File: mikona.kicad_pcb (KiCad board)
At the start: 4 copper layers, 50 x 40 mm, 83 parts, among them J1 TC2030-IDC-NL, Q1 BSC109N10NS3 G, Q2 FQD5N60C, Q3 IGB50N60T, Q4 IGB50N60T, U1 LT3750EMS#PBF, U10 24CW1280T, U2 ZXGD3009E6, U3 MCP6V51, U4 STM32F103T6U6A, U5 Texas Instruments UCC27624DR, U6 KTD2052, U7 TLT9251VLE, U8 MAX17671FATB+, U9 MCP4562T-503E/MF

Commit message: Cleanup the project after moving to KiCad.
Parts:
- removed R18, R27, R28, R29, R30: 100K, Vault:RESC1005X40X25ML10T10
- removed R20, R21: 10, Vault:RESC1005X40X25NL05T05
- removed R23: 787K, Vault:RESC1005X40X25LL05T05
- removed R25, R26: 4.7K, Vault:RESC1005X40X25NL05T05
- added C28: 22uF, Capacitor_SMD:C_0805_2012Metric_Pad1.18x1.45mm_HandSolder, B.Cu at (184.1, 114.2)
- added C29: 2.2uF, Capacitor_SMD:C_0402_1005Metric_Pad0.74x0.62mm_HandSolder, B.Cu at (190.4, 114.5)
- added D5: SMBJ13CA, Diode_SMD:D_SMB_Handsoldering, B.Cu at (176.3, 92.2)
- added RN1: 100K, Resistor_SMD:R_Array_Convex_2x0402, F.Cu at (109.8, 103.2)
- added RN2: 4.7K, Resistor_SMD:R_Array_Convex_2x0402, F.Cu at (107.5, 106.5)
- added RN3: 100K, Resistor_SMD:R_Array_Convex_2x0402, F.Cu at (107.2, 108.5)
- added U11: MIC5528-3.3, MIC5528-3.3YMT-TR:SON40P120X120X60-7N, B.Cu at (188.7, 114.4)
- C1, C12: value 10 µF -> 10µF; footprint Vault:RESC2013X55X40ML15T20 -> Capacitor_SMD:C_0805_2012Metric_Pad1.18x1.45mm_HandSolder
- C10, C14, C15, C16, C18, C19, C20, C27: footprint Vault:PCB-ya5qsrmvtd5pjczft90h-1 -> Capacitor_SMD:C_0402_1005Metric_Pad0.74x0.62mm_HandSolder
- C11: footprint Vault:PCB-lqeomw61a722wi99q4vw-1 -> Capacitor_SMD:C_0402_1005Metric_Pad0.74x0.62mm_HandSolder
- C13: value 100nF -> 10µF; footprint Vault:PCB-ya5qsrmvtd5pjczft90h-1 -> Capacitor_SMD:C_0805_2012Metric_Pad1.18x1.45mm_HandSolder
- C17: footprint Vault:PCB-8tuutlkq7p1aj3t2dfdp-1 -> Capacitor_SMD:C_0402_1005Metric_Pad0.74x0.62mm_HandSolder
- C2: footprint Vault:PCB-nvrhrmzuvt0gp2xpn124-1 -> Capacitor_SMD:C_1206_3216Metric_Pad1.33x1.80mm_HandSolder
- C21: footprint Vault:PCB-lqeomw61a722wi99q4vw-1 -> Capacitor_SMD:C_0805_2012Metric_Pad1.18x1.45mm_HandSolder
- C22: value 10 µF -> 100nF; footprint Vault:RESC2013X55X40ML15T20 -> Capacitor_SMD:C_0402_1005Metric_Pad0.74x0.62mm_HandSolder; moved to F.Cu
- C23: footprint Vault:PCB-cxx7a5qu32qlaf9eltup-1 -> Capacitor_SMD:C_0402_1005Metric_Pad0.74x0.62mm_HandSolder
- C24: value 1uF -> 10uF; footprint Vault:CAPC1608X90X35ML15T15 -> Capacitor_SMD:C_0603_1608Metric_Pad1.08x0.95mm_HandSolder
- C25: footprint Vault:CAPC1608X90X35LL10T15 -> Capacitor_SMD:C_0402_1005Metric_Pad0.74x0.62mm_HandSolder
- C26: value 4.7uF -> 22uF; footprint Vault:CAPC1608X90X35NL10T15 -> Capacitor_SMD:C_0805_2012Metric_Pad1.18x1.45mm_HandSolder
- C3, C9: footprint Vault:PCB-fmxckod8eunvntzfi285-1 -> Capacitor_SMD:C_0402_1005Metric_Pad0.74x0.62mm_HandSolder
- C4, C5, C6: value 22 uF -> 22uF; footprint Vault:CAPC3225X270X30NL30 -> Capacitor_SMD:C_1210_3225Metric_Pad1.33x2.70mm_HandSolder
- C7: footprint Vault:PCBComponent_1 -> Capacitor_SMD:CP_Elec_8x11.9
- C8: footprint Vault:PCB-hxcivebo8v2ep67jp7i8-1 -> Capacitor_SMD:C_1812_4532Metric_Pad1.57x3.40mm_HandSolder
- D1: footprint Vault:PCB-1avwftqup47cwryg2qb4-1 -> Diode_SMD:D_SMB_Handsoldering
- D2: value SP712 -> SMBJ13CA; footprint Vault:ONSC-SOT-23-3-318-08_V -> Diode_SMD:D_SMB_Handsoldering
- D3: value onsemi FFSB2065BDN-F085 -> FFSB2065BDN-F085; footprint Vault:ONSC-TO-263-2L-3_V -> Package_TO_SOT_SMD:TO-263-2
- D4: value Lite-On LTST-C19HE1WT -> RGB; footprint Vault:PCB-52d9enhv62acg8agpph7-1 -> LED_SMD:LED_LiteOn_LTST-C19HE1WT
- F1: footprint Vault:PCB-177u4nhbl1z1alzoqvvf-1 -> Fuse:Fuse_0603_1608Metric_Pad1.05x0.95mm_HandSolder
- FB2: value 100 -> FerriteBead_Small; footprint Vault:MURA-BLM18KG_TN-B60-CHIP-2_V3 -> Resistor_SMD:R_0603_1608Metric_Pad0.98x0.95mm_HandSolder
- J1: footprint Vault:PCB-ltb50y2q1twco73v61fe-1 -> Connector:Tag-Connect_TC2030-IDC-NL_2x03_P1.27mm_Vertical
- JCAP1: renamed from JCAP; footprint Vault:PCB-udjxl8ocgqbbk8gqzxxz-1 -> 1054291104:MOLEX_1054291104
- JMAG1: renamed from JMAG; footprint Vault:PCB-udjxl8ocgqbbk8gqzxxz-1 -> 1054291104:MOLEX_1054291104
- JMAIN1: renamed from JMAIN; footprint Vault:PCB-udjxl8ocgqbbk8gqzxxz-1 -> 1054291104:MOLEX_1054291104
- L1: value Coilcraft DA2034-ALB -> DA2034-AL; footprint Vault:LCC18 -> DA2034-AL:DA2034-AL
- L2: value 68.0µH -> 4.7uH; footprint Vault:PCB-o31o4oqkad523pnvsppd-1 -> Inductor_SMD:L_Taiyo-Yuden_NR-50xx_HandSoldering
- Q1: value BSC109N10NS3 G -> BSC109N10NS3G; footprint Vault:INF-PG-TDSON-8-1_V -> Package_TO_SOT_SMD:TDSON-8-1
- Q2: value FQD5N60C -> STN3N40K3; footprint Vault:PCB-yetu4xpugvmduszhgs8y-1 -> Package_TO_SOT_SMD:SOT-223
- Q3, Q4: footprint Vault:INF-PG-TO-263-3-2_A_M -> Package_TO_SOT_SMD:TO-263-2
- R1: footprint Vault:RESC1005X40X25ML05T05 -> Resistor_SMD:R_0402_1005Metric_Pad0.72x0.64mm_HandSolder
- R10, R11, R9: footprint Vault:Panasonic ERJ-1TNF22R6U-Footprint-1 -> Resistor_SMD:R_2512_6332Metric_Pad1.40x3.35mm_HandSolder
- R12, R2, R3, R6: footprint Vault:RESC1005X40X25ML10T10 -> Resistor_SMD:R_0402_1005Metric_Pad0.72x0.64mm_HandSolder
- R13: value 100K -> 0; footprint Vault:RESC1005X40X25ML10T10 -> Resistor_SMD:R_0402_1005Metric_Pad0.72x0.64mm_HandSolder
- R14: footprint Vault:SMD0603GRID25PAD90 -> Resistor_SMD:R_0603_1608Metric_Pad0.98x0.95mm_HandSolder
- R15: footprint Vault:ERJ-PB3B1002V -> Resistor_SMD:R_0603_1608Metric_Pad0.98x0.95mm_HandSolder
- R16: footprint Vault:CAPC1608X90X35LL15T15 -> Resistor_SMD:R_0603_1608Metric_Pad0.98x0.95mm_HandSolder
- R17: value 0 -> 10; footprint Vault:RESC1005X40X25ML05T10 -> Resistor_SMD:R_0402_1005Metric_Pad0.72x0.64mm_HandSolder
- R19: footprint Vault:RESC1005X37X25LL05T10 -> Resistor_SMD:R_0402_1005Metric_Pad0.72x0.64mm_HandSolder
- R22, R5: footprint Vault:RESC1005X40X25ML05T10 -> Resistor_SMD:R_0402_1005Metric_Pad0.72x0.64mm_HandSolder
- R24: value 3.32M -> 0; footprint Vault:RESC1005X40X25NL05T05 -> Resistor_SMD:R_0402_1005Metric_Pad0.72x0.64mm_HandSolder; moved to F.Cu
- R4: value 100K -> 10; footprint Vault:RESC1005X40X25ML10T10 -> Resistor_SMD:R_0402_1005Metric_Pad0.72x0.64mm_HandSolder
- R7: footprint Vault:PCB-lktu9k9qvhh1xmnw65nf-1 -> Resistor_SMD:R_0805_2012Metric_Pad1.20x1.40mm_HandSolder
- R8: footprint Vault:RESC1005X40X25NL05T05 -> Resistor_SMD:R_0402_1005Metric_Pad0.72x0.64mm_HandSolder
- U1: value LT3750EMS#PBF -> LT3750EMSTR; footprint Vault:LT-MS-10_N -> LT3750EMSTR:MSOP-10_MS
- U10: value 24CW1280T -> MX25V1006FZUI; footprint Vault:PCB-du7oa82jyfofml92o6ch-1 -> MX25V1006FZUI:MX25V1006FZUI
- U2: footprint Vault:MF06A_N -> Package_TO_SOT_SMD:SOT-23-6
- U3: value MCP6V51 -> NCS325; footprint Vault:ADI-RJ-5_L -> Package_TO_SOT_SMD:SOT-23-5
- U4: value STM32F103T6U6A -> STM32F042G6Ux; footprint Vault:STM-VFQFPN36_L -> Package_DFN_QFN:QFN-28_4x4mm_P0.5mm
- U5: value Texas Instruments UCC27624DR -> IX4427MTR; footprint Vault:SOIC-OA8_L -> Package_DFN_QFN:VDFN-8-1EP_2x2mm_P0.5mm_EP0.9x1.7mm
- U6: value KTD2052 -> KTD2026EWE-TR; footprint Vault:PCB-1zdkv4te5dlcf1e3m0hc-1 -> KTD2026EWE-TR:SON40P150X150X55-9N
- U7: value TLT9251VLE -> ATA6561-GBQW; footprint Vault:PCB-is4r40753zstvrjiqh7i-1 -> ATA6561-GBQW:SON65P300X300X100-9N
- U8: value MAX17671FATB+ -> AP63205WU; footprint Vault:T1033+1_V -> Package_TO_SOT_SMD:TSOT-23-6
- U9: value MCP4562T-503E/MF -> MCP4562T-503E; footprint Vault:DFN-MF8 -> MCP4562T-503E_MF:SON65P300X300X100-9N-D
- moved R13 51.6 mm to (188.7, 115.8), turned to 180 degrees
- moved C22 38.5 mm to (183.8, 117.6)
- moved R4 27.1 mm to (153.5, 100.0)
- moved FB2 23.9 mm to (189.7, 118.1)
- moved C24 21.7 mm to (188.1, 118.1)
- moved R17 19.6 mm to (153.5, 99.0)
- moved D2 19.2 mm to (176.1, 103.8), turned to 90 degrees
- moved R24 17.9 mm to (186.1, 118.6), turned to -90 degrees
- moved C25 17.0 mm to (188.7, 113.1), turned to 0 degrees
- moved C26 16.4 mm to (186.1, 114.2), turned to 90 degrees
- moved U8 15.6 mm to (185.0, 118.1), turned to 180 degrees
- moved L2 12.5 mm to (180.2, 116.0), turned to 90 degrees
- moved JCAP1 3.05 mm to (166.7, 90.8)
- moved JMAG1 2.97 mm to (166.7, 98.5)
- moved JMAIN1 2.59 mm to (166.7, 120.3)
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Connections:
- net NetD1_2 renamed Net-(D1-A)
- net NetD4_1 renamed Net-(D4-RK)
- net NetF1_1 renamed Net-(F1-Pad1)
- net NetQ1_4 renamed Net-(Q1-G)
- net NetR23_2 renamed Net-(U8-EN)
- net RVOUT renamed /Power/RVOUT
- C1 pad 1: GND -> +24V
- C1 pad 2: VIN -> GND
- C10 pad 1: GND -> +3.3V
- C10 pad 2: 3V3 -> GND
- C11 pad 1: GND -> Net-(U4-NRST)
- C11 pad 2: NetC11_2 -> GND
- C12 pad 2: 5V -> +5V
- C13 pad 1: GND -> +24V
- C13 pad 2: 3V3 -> GND
- C14 pad 1: GND -> +3.3V
- C14 pad 2: 3V3 -> GND
- C15 pad 1: GND -> +3.3V
- C15 pad 2: 3V3 -> GND
- C16 pad 1: GND -> +3.3V
- C16 pad 2: 3V3 -> GND
- C17 pad 1: GND -> +3.3V
- C17 pad 2: 3V3 -> GND
- C18 pad 1: GND -> +3.3V
- C18 pad 2: 3V3 -> GND
- C19 pad 1: GND -> +3.3V
- C19 pad 2: 3V3 -> GND
- C2 pad 1: NetC2_1 -> GND
- C2 pad 2: GND -> Net-(U1-VTRANS)
- C20 pad 1: GND -> +5V
- C20 pad 2: 5V -> GND
- C21 pad 1: GND -> +24V
- C21 pad 2: VIN -> GND
- C22 pad 1: GND -> Net-(U8-BST)
- C22 pad 2: VIN -> Net-(U8-SW)
- C23 pad 1: GND -> +24V
- C23 pad 2: VIN -> GND
- C24 pad 1: GND -> Net-(U8-IN)
- C24 pad 2: NetC24_2 -> GND
- C25 pad 1: GND -> +5V
- C25 pad 2: 3V3 -> GND
- C26 pad 1: GND -> +5V
- C26 pad 2: 5V -> GND
- C27 pad 1: GND -> +3.3V
- C27 pad 2: 3V3 -> GND
- C3 pad 1: GND -> Net-(U1-RBG)
- C3 pad 2: NetC3_2 -> GND
- C4 pad 2: VIN -> +24V
- C5 pad 2: VIN -> +24V
- C6 pad 2: VIN -> +24V
- C7 pad 1: VIN -> +24V
- C8 pad 1: GND -> +3.3V
- C8 pad 2: VOUT -> GND
- C9 pad 1: GND -> Net-(U3-+)
- C9 pad 2: NetC9_2 -> GND
- D1 pad 1: VOUT -> +3.3V
- D2 pad 1: NetD2_1 -> Net-(D2-A1)
- D2 pad 2: NetD2_2 -> GND
- D3 pad 1: MAGNET_B_2 -> /MAGNET_A_2
- D3 pad 2: VOUT -> +3.3V
- D3 pad 3: MAGNET_A_2 -> /MAGNET_B_2
- D4 pad 2: NetD4_2 -> Net-(D4-GK)
- D4 pad 3: NetD4_3 -> Net-(D4-BK)
- D4 pad 4: NetD4_4 -> +5V
- F1 pad 2: VIN -> +24V
- FB2 pad 1: VIN -> +24V
- FB2 pad 2: NetC24_2 -> Net-(U8-IN)
- J1 pad 1: 3V3 -> +3.3V
- J1 pad 2: SWDIO -> /Logic/SWDIO
- J1 pad 3: SW_NRST -> /Logic/SW_NRST
- J1 pad 4: SWCLK -> /Logic/SWCLK
- J1 pad 6: SWO -> unconnected-(J1-SWO-Pad6)
- JCAP1 pad 3: VOUT -> +3.3V
- JCAP1 pad 4: VOUT -> +3.3V
- JMAG1 pad 1: MAGNET_A_2 -> /MAGNET_A_2
- JMAG1 pad 2: MAGNET_B_2 -> /MAGNET_B_2
- JMAG1 pad 3: VOUT -> +3.3V
- JMAG1 pad 4: VOUT -> +3.3V
- JMAIN1 pad 1: CAN_P -> /CAN_P
- JMAIN1 pad 2: CAN_N -> /CAN_N
- L1 pad 10: NMOS_DRAIN -> /Power/NMOS_DRAIN
- L1 pad 3: VIN -> +24V
- L1 pad 4: VIN -> +24V
- L1 pad 5: VIN -> +24V
- L1 pad 6: VIN -> +24V
- L1 pad 7: NMOS_DRAIN -> /Power/NMOS_DRAIN
- L1 pad 8: NMOS_DRAIN -> /Power/NMOS_DRAIN
- L1 pad 9: NMOS_DRAIN -> /Power/NMOS_DRAIN
- L2 pad 1: NetL2_1 -> Net-(U8-SW)
- L2 pad 2: 5V -> +5V
- Q1 pad 1: NetQ1_1 -> Net-(U1-SOURCE)
- Q1 pad 2: NetQ1_1 -> Net-(U1-SOURCE)
- Q1 pad 3: NetQ1_1 -> Net-(U1-SOURCE)
- Q1 pad 5: NMOS_DRAIN -> /Power/NMOS_DRAIN
- Q2 pad 1: NetQ2_1 -> Net-(Q2-G)
- Q2 pad 4: NetQ2_4 -> Net-(Q2-D-Pad2)
- Q3 pad 1: NetD2_1 -> Net-(D2-A1)
- Q3 pad 2: MAGNET_A_2 -> /MAGNET_A_2
- Q4 pad 1: NetD2_2 -> Net-(D5-A1)
- Q4 pad 2: MAGNET_B_2 -> /MAGNET_B_2
- R1 pad 1: NetR1_1 -> /Power/NMOS_DRAIN
- R1 pad 2: NMOS_DRAIN -> Net-(U1-RDCM)
- R10 pad 1: VOUT -> +3.3V
- R10 pad 2: NetQ2_4 -> Net-(Q2-D-Pad2)
- R11 pad 1: VOUT -> +3.3V
- R11 pad 2: NetQ2_4 -> Net-(Q2-D-Pad2)
- R12 pad 1: GND -> Net-(U2-SINK)
- R12 pad 2: NetR8_1 -> GND
- R13 pad 1: GND -> +5V
- R13 pad 2: DISCHARGE -> Net-(U11-EN)
- R14 pad 1: NetR14_1 -> +3.3V
- R14 pad 2: VOUT -> Net-(R14-Pad2)
- R15 pad 1: GND -> Net-(R14-Pad2)
- R15 pad 2: NetR14_1 -> GND
- R16 pad 1: NetR14_1 -> Net-(U3-+)
- R16 pad 2: NetC9_2 -> Net-(R14-Pad2)
- R17 pad 1: NetC11_2 -> Net-(D5-A1)
- R17 pad 2: REG_NRST -> Net-(U5-OUT_B)
- R19 pad 1: CAN_N -> /CAN_P
- R19 pad 2: CAN_P -> /CAN_N
- R2 pad 1: 3V3 -> +5V
- R2 pad 2: DONE -> Net-(U6-ST)
- R22 pad 1: SW_NRST -> Net-(U4-NRST)
- R22 pad 2: NetC11_2 -> /Logic/SW_NRST
- R24 pad 2: NetC24_2 -> Net-(U8-IN)
- R3 pad 1: NetR3_1 -> /Power/NMOS_DRAIN
- R3 pad 2: NMOS_DRAIN -> Net-(U9-P0B)
- R4 pad 1: GND -> Net-(D2-A1)
- R4 pad 2: CHARGE -> Net-(U5-OUT_A)
- R5 pad 1: VIN -> +24V
- R5 pad 2: NetC2_1 -> Net-(U1-VTRANS)
- R6 pad 1: GND -> Net-(U1-RBG)
- R6 pad 2: NetC3_2 -> GND
- R7 pad 1: GND -> Net-(U1-SOURCE)
- R7 pad 2: NetQ1_1 -> GND
- R8 pad 1: NetR8_1 -> Net-(Q2-G)
- R8 pad 2: NetQ2_1 -> Net-(U2-SINK)
- R9 pad 1: VOUT -> +3.3V
- R9 pad 2: NetQ2_4 -> Net-(Q2-D-Pad2)
- U1 pad 1: NetC2_1 -> Net-(U1-VTRANS)
- U1 pad 10: NetC3_2 -> Net-(U1-RBG)
- U1 pad 2: DONE -> /Logic/DONE
- U1 pad 3: CHARGE -> /Logic/CHARGE
- U1 pad 4: VIN -> +24V
- U1 pad 6: NetQ1_1 -> Net-(U1-SOURCE)
- U1 pad 8: NetR1_1 -> Net-(U1-RDCM)
- U10 pad 1: SCL -> /Logic/FLASH_CS
- U10 pad 2: GND -> /Logic/MISO
- U10 pad 3: SDA -> /Logic/FLASH_WP
- U10 pad 4: 3V3 -> GND
- U10 pad 5: (no net) -> /Logic/MOSI
- U2 pad 1: VIN -> +24V
- U2 pad 2: DISCHARGE -> /Logic/DISCHARGE
- U2 pad 4: NetR8_1 -> Net-(U2-SINK)
- U2 pad 5: (no net) -> unconnected-(U2-NC-Pad5)
- U2 pad 6: NetR8_1 -> Net-(U2-SINK)
- U3 pad 1: VOUT_ADC -> /Logic/VOUT_ADC
- U3 pad 3: NetC9_2 -> Net-(U3-+)
- U3 pad 4: VOUT_ADC -> /Logic/VOUT_ADC
- U3 pad 5: 3V3 -> +3.3V
- U4 pad 1: 3V3 -> unconnected-(U4-PB8-Pad1)
- U4 pad 10: (no net) -> /Logic/KICK_B
- U4 pad 11: (no net) -> /Logic/KICK_A
- U4 pad 12: DISCHARGE -> unconnected-(U4-PA6-Pad12)
- U4 pad 13: VOUT_ADC -> unconnected-(U4-PA7-Pad13)
- U4 pad 14: KICK_B -> unconnected-(U4-PB0-Pad14)
- U4 pad 15: KICK_A -> /Logic/CAN_STB
- U4 pad 16: KICK_A_EN -> GND
- U4 pad 17: KICK_B_EN -> +3.3V
- U4 pad 18: GND -> +3.3V
- U4 pad 19: 3V3 -> /Logic/CAN_RX
- U4 pad 2: (no net) -> /Logic/SDA
- U4 pad 20: (no net) -> /Logic/CAN_TX
- U4 pad 21: (no net) -> /Logic/SWDIO
- U4 pad 22: CAN_STB -> /Logic/SWCLK
- U4 pad 23: CAN_RX -> unconnected-(U4-PA15-Pad23)
- U4 pad 24: CAN_TX -> /Logic/SCK
- U4 pad 25: SWDIO -> /Logic/MISO
- U4 pad 26: GND -> /Logic/MOSI
- U4 pad 27: 3V3 -> /Logic/FLASH_CS
- U4 pad 28: SWCLK -> /Logic/FLASH_WP
- U4 pad 3: (no net) -> /Logic/SCL
- U4 pad 4: NetC11_2 -> Net-(U4-NRST)
- U4 pad 5: GND -> +3.3V
- U4 pad 6: 3V3 -> /Logic/CHARGE
- U4 pad 7: CHARGE -> /Logic/DONE
- U4 pad 8: DONE -> /Logic/DISCHARGE
- U4 pad 9: (no net) -> /Logic/VOUT_ADC
- U5 pad 1: KICK_A_EN -> unconnected-(U5-NC-Pad1)
- U5 pad 2: KICK_A -> /Logic/KICK_A
- U5 pad 4: KICK_B -> /Logic/KICK_B
- U5 pad 5: NetR21_1 -> Net-(U5-OUT_B)
- U5 pad 6: VIN -> +24V
- U5 pad 7: NetR20_1 -> Net-(U5-OUT_A)
- U5 pad 8: KICK_B_EN -> unconnected-(U5-NC-Pad8)
- U6 pad 1: SCL -> Net-(U6-ST)
- U6 pad 2: SDA -> Net-(D4-BK)
- U6 pad 3: NetD4_3 -> Net-(D4-GK)
- U6 pad 5: NetD4_2 -> +5V
- U6 pad 6: NetD4_4 -> /Logic/SCL
- U6 pad 7: GND -> /Logic/SDA
- U6 pad 8: 5V -> GND
- U7 pad 1: CAN_TX -> /Logic/CAN_TX
- U7 pad 3: 5V -> +5V
- U7 pad 4: CAN_RX -> /Logic/CAN_RX
- U7 pad 5: 3V3 -> +3.3V
- U7 pad 6: CAN_N -> /CAN_N
- U7 pad 7: CAN_P -> /CAN_P
- U7 pad 8: CAN_STB -> /Logic/CAN_STB
- U8 pad 1: NetC24_2 -> +5V
- U8 pad 3: (no net) -> Net-(U8-IN)
- U8 pad 4: 5V -> GND
- U8 pad 5: 3V3 -> Net-(U8-SW)
- U8 pad 6: 5V -> Net-(U8-BST)
- U9 pad 2: SCL -> /Logic/SCL
- U9 pad 3: SDA -> /Logic/SDA
- U9 pad 6: NetR3_1 -> Net-(U9-P0B)
- U9 pad 8: 3V3 -> +3.3V
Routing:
- net (no net): track 0.00 -> 224.5 mm, vias 0 -> 14
- net MAGNET_B_2: track 34.8 -> 0.00 mm, vias 2 -> 0
- net VOUT: track 34.6 -> 0.00 mm
- net REG_NRST: track 33.3 -> 0.00 mm, vias 1 -> 0
- net SCL: track 26.9 -> 0.00 mm, vias 2 -> 0
- net VIN: track 22.5 -> 0.00 mm
- net /Logic/DISCHARGE: track 0.00 -> 22.2 mm
- net DISCHARGE: track 21.5 -> 0.00 mm
- net NMOS_DRAIN: track 20.6 -> 0.00 mm
- net SDA: track 20.5 -> 0.00 mm, vias 2 -> 0
- net DONE: track 19.5 -> 0.00 mm
- net /Logic/DONE: track 0.00 -> 19.5 mm
- net CHARGE: track 19.5 -> 0.00 mm
- net /Logic/CHARGE: track 0.00 -> 19.5 mm
- net /Logic/VOUT_ADC: track 0.00 -> 17.6 mm
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- removed copper zone on B.Cu, net NetC24_2
- removed copper zone on B.Cu, net VIN

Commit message: Add missing 3d models.
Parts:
- D4: footprint LED_SMD:LED_LiteOn_LTST-C19HE1WT -> LTST-C19HE1WT:LED_LiteOn_LTST-C19HE1WT
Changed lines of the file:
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@@
     (pad "9" smd rect (at 0 0 180) (size 1.6 2.4) (layers "F.Cu" "F.Paste" "F.Mask")
       (net 1 "GND") (pinfunction "EP") (pintype "passive"))
-    (model "MCP4562T-503E_MF.stp"
+    (model "${KIPRJMOD}/libraries/MCP4562T-503E_MF/DFN8_3x3MC_MCH.step"
       (offset (xyz 0 0 0))
       (scale (xyz 1 1 1))
@@
     (pad "S2" smd rect (at 3.055 0.475 270) (size 1.1 10.5) (layers "F.Cu" "F.Paste")
       (net 30 "unconnected-(JMAIN1-SHIELD2-PadS2)") (pinfunction "SHIELD2") (pintype "passive+no_connect"))
+    (model "${KIPRJMOD}/libraries/1054291104/1054291104.step"
+      (offset (xyz 0 0 0))
+      (scale (xyz 1 1 1))
+      (rotate (xyz 0 0 0))
+    )
   )
   (footprint "Resistor_SMD:R_0805_2012Metric_Pad1.20x1.40mm_HandSolder" (layer "F.Cu")
@@
     (pad "9" smd rect (at 0 0 270) (size 0.75 1.25) (layers "F.Cu" "F.Paste" "F.Mask")
       (net 1 "GND") (pinfunction "EP") (pintype "power_in"))
-    (model "KTD2026EWE-TR.stp"
+    (model "${KIPRJMOD}/libraries/KTD2026EWE-TR/UTDFN8_1P5X1P5_KIN.step"
       (offset (xyz 0 0 0))
       (scale (xyz 1 1 1))
@@
     )
   )
-  (footprint "LED_SMD:LED_LiteOn_LTST-C19HE1WT" (layer "F.Cu")
+  (footprint "LTST-C19HE1WT:LED_LiteOn_LTST-C19HE1WT" (layer "F.Cu")
     (at 142.0011 122.0036 -90)
     (descr "LiteOn RGB LED; https://optoelectronics.liteon.com/upload/download/DS22-2008-0044/LTST-C19HE1WT.pdf")
@@
     (pad "4" smd rect (at -0.425 0.725 270) (size 0.65 0.85) (layers "F.Cu" "F.Paste" "F.Mask")
       (net 7 "+5V") (pinfunction "A") (pintype "passive"))
-    (model "${KICAD6_3DMODEL_DIR}/LED_SMD.3dshapes/LED_LiteOn_LTST-C19HE1WT.wrl"
+    (model "${KIPRJMOD}/libraries/LTST-C19HE1WT/LTST-C19HE1WT.STEP"
       (offset (xyz 0 0 0))
       (scale (xyz 1 1 1))
-      (rotate (xyz 0 0 0))
+      (rotate (xyz -90 0 -90))
     )
   )
@@
     (pad "S2" smd rect (at 3.055 0.475 270) (size 1.1 10.5) (layers "F.Cu" "F.Paste")
       (net 26 "unconnected-(JMAG1-SHIELD2-PadS2)") (pinfunction "SHIELD2") (pintype "passive+no_connect"))
+    (model "${KIPRJMOD}/libraries/1054291104/1054291104.step"
+      (offset (xyz 0 0 0))
+      (scale (xyz 1 1 1))
+      (rotate (xyz 0 0 0))
+    )
   )
   (footprint "Capacitor_SMD:C_0402_1005Metric_Pad0.74x0.62mm_HandSolder" (layer "F.Cu")
@@
     (pad "12" smd rect (at 13.46 -7.5 270) (size 3.3 1.27) (layers "F.Cu" "F.Paste" "F.Mask")
       (net 1 "GND") (pinfunction "12") (pintype "passive"))
+    (model "${KIPRJMOD}/libraries/DA2034-AL/Coilcraft-DA2034-AL.step"
+      (offset (xyz 0 0 0))
+      (scale (xyz 1 1 1))
+      (rotate (xyz -90 0 0))
+    )
   )
   (footprint "Connector:Tag-Connect_TC2030-IDC-NL_2x03_P1.27mm_Vertical" (layer "F.Cu")
@@
     (pad "S2" smd rect (at 3.055 0.475 270) (size 1.1 10.5) (layers "F.Cu" "F.Paste")
       (net 24 "unconnected-(JCAP1-SHIELD2-PadS2)") (pinfunction "SHIELD2") (pintype "passive+no_connect"))
+    (model "${KIPRJMOD}/libraries/1054291104/1054291104.step"
+      (offset (xyz 0 0 0))
+      (scale (xyz 1 1 1))
+      (rotate (xyz 0 0 0))
+    )
   )
   (footprint "Capacitor_SMD:C_0402_1005Metric_Pad0.74x0.62mm_HandSolder" (layer "F.Cu")
@@
     (pad "9" smd rect (at 0 0) (size 1.6 2.4) (layers "B.Cu" "B.Mask")
       (net 1 "GND") (pinfunction "EXP") (pintype "power_in"))
+    (model "${KIPRJMOD}/libraries/ATA6561-GBQW/vdfn8-bbb.STEP"
+      (offset (xyz 0 0 0))
+      (scale (xyz 0.5 0.5 0.5))
+      (rotate (xyz 0 0 0))
+    )
   )
   (footprint "Capacitor_SMD:C_0402_1005Metric_Pad0.74x0.62mm_HandSolder" (layer "B.Cu")
@@
         (effects (font (size 1 1) (thickness 0.15)) (justify mirror))
     )
-    (fp_text user "Copyright 2021 Accelerated Designs. All rights reserved." (at 0 0) (layer "Cmts.User")
-        (effects (font (size 0.127 0.127) (thickness 0.002)))
-    )
-    (fp_text user "0.01in/0.255mm" (at 4.4934 0.762) (layer "Cmts.User")
+    (fp_text user "0.02in/0.508mm" (at -4.4934 0.508) (layer "Cmts.User")
         (effects (font (size 1 1) (thickness 0.15)))
     )
-    (fp_text user "0.114in/2.891mm" (at 0 3.4671) (layer "Cmts.User")
+    (fp_text user "0.012in/0.305mm" (at 0 -4.1021) (layer "Cmts.User")
         (effects (font (size 1 1) (thickness 0.15)))
     )
@@
         (effects (font (size 1 1) (thickness 0.15)))
     )
-    (fp_text user "0.02in/0.508mm" (at -4.4934 0.508) (layer "Cmts.User")
+    (fp_text user "0.067in/1.702mm" (at 3.9624 0) (layer "Cmts.User")
         (effects (font (size 1 1) (thickness 0.15)))
     )
-    (fp_text user "0.012in/0.305mm" (at 0 -4.1021) (layer "Cmts.User")
+    (fp_text user "0.114in/2.891mm" (at 0 3.4671) (layer "Cmts.User")
         (effects (font (size 1 1) (thickness 0.15)))
     )
-    (fp_text user "0.067in/1.702mm" (at 3.9624 0) (layer "Cmts.User")
+    (fp_text user "Copyright 2021 Accelerated Designs. All rights reserved." (at 0 0) (layer "Cmts.User")
+        (effects (font (size 0.127 0.127) (thickness 0.002)))
+    )
+    (fp_text user "0.01in/0.255mm" (at 4.4934 0.762) (layer "Cmts.User")
         (effects (font (size 1 1) (thickness 0.15)))
     )
@@
     (pad "9" smd rect (at 0 0 180) (size 0.3048 1.7018) (layers "B.Cu" "B.Paste" "B.Mask")
       (net 1 "GND") (pinfunction "GND") (pintype "power_in"))
+    (model "${KIPRJMOD}/libraries/MX25V1006FZUI/USON8L_MAC.step"
+      (offset (xyz 0 0 0))
+      (scale (xyz 1 1 1))
+      (rotate (xyz 0 0 0))
+    )
   )
   (footprint "Resistor_SMD:R_0402_1005Metric_Pad0.72x0.64mm_HandSolder" (layer "B.Cu")
@@
     (pad "10" smd rect (at 2.1844 1.00076 180) (size 1.397 0.2794) (layers "B.Cu" "B.Paste" "B.Mask")
       (net 4 "Net-(U1-RBG)") (pinfunction "RBG") (pintype "output"))
+    (model "${KIPRJMOD}/libraries/LT3750EMSTR/MSOP-10_MS_LIT.step"
+      (offset (xyz 0 0 0))
+      (scale (xyz 1 1 1))
+      (rotate (xyz 0 0 0))
+    )
   )
   (footprint "Capacitor_SMD:C_0805_2012Metric_Pad1.18x1.45mm_HandSolder" (layer "B.Cu")
@@
     (pad "7" smd rect (at 0 0 180) (size 0.3 0.94) (layers "B.Cu" "B.Mask")
       (net 1 "GND") (pinfunction "GND") (pintype "power_in"))
+    (model "${KIPRJMOD}/libraries/MIC5528-3.3YMT-TR/TDFN6_1P2X1P2_MCH.step"
+      (offset (xyz 0 0 0))
+      (scale (xyz 1 1 1))
+      (rotate (xyz 0 0 0))
+    )
   )
   (footprint "Package_TO_SOT_SMD:TSOT-23-6" (layer "B.Cu")

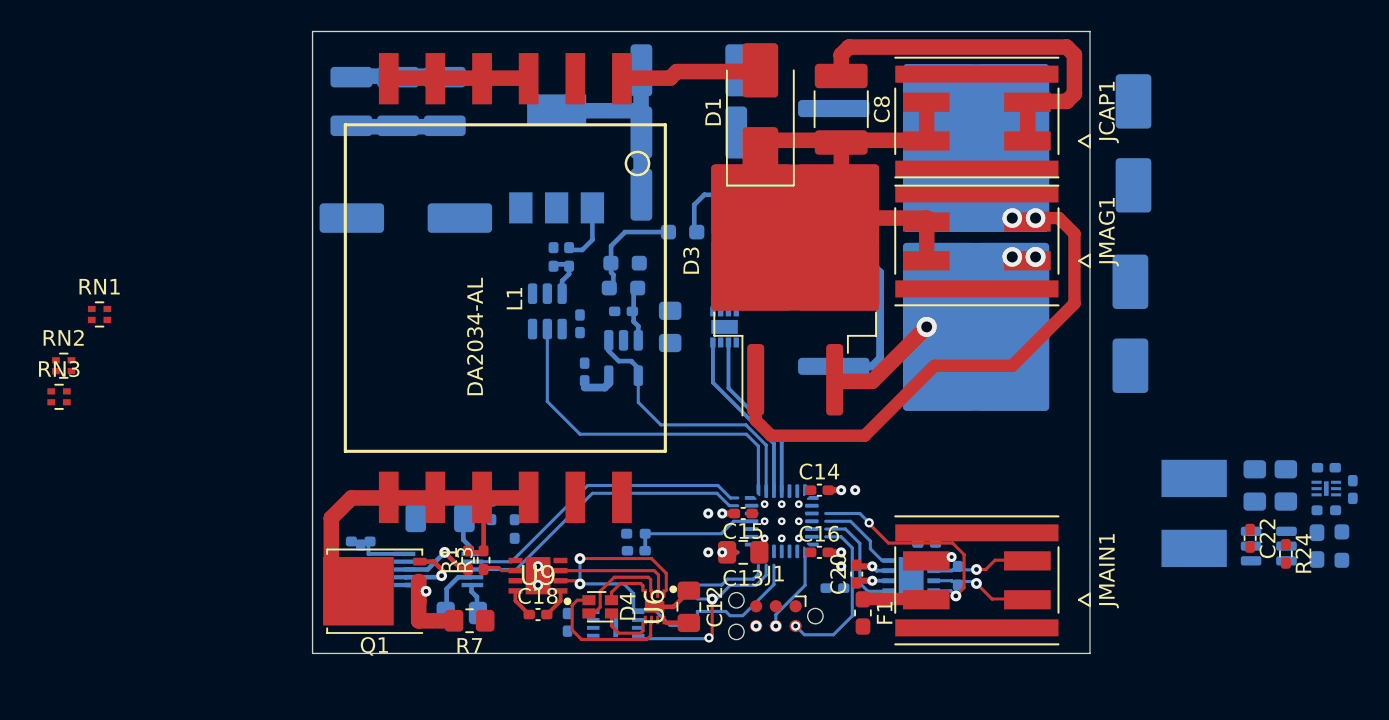
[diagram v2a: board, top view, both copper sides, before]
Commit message: Finish the layout, remove old routings, and setup internal planes.
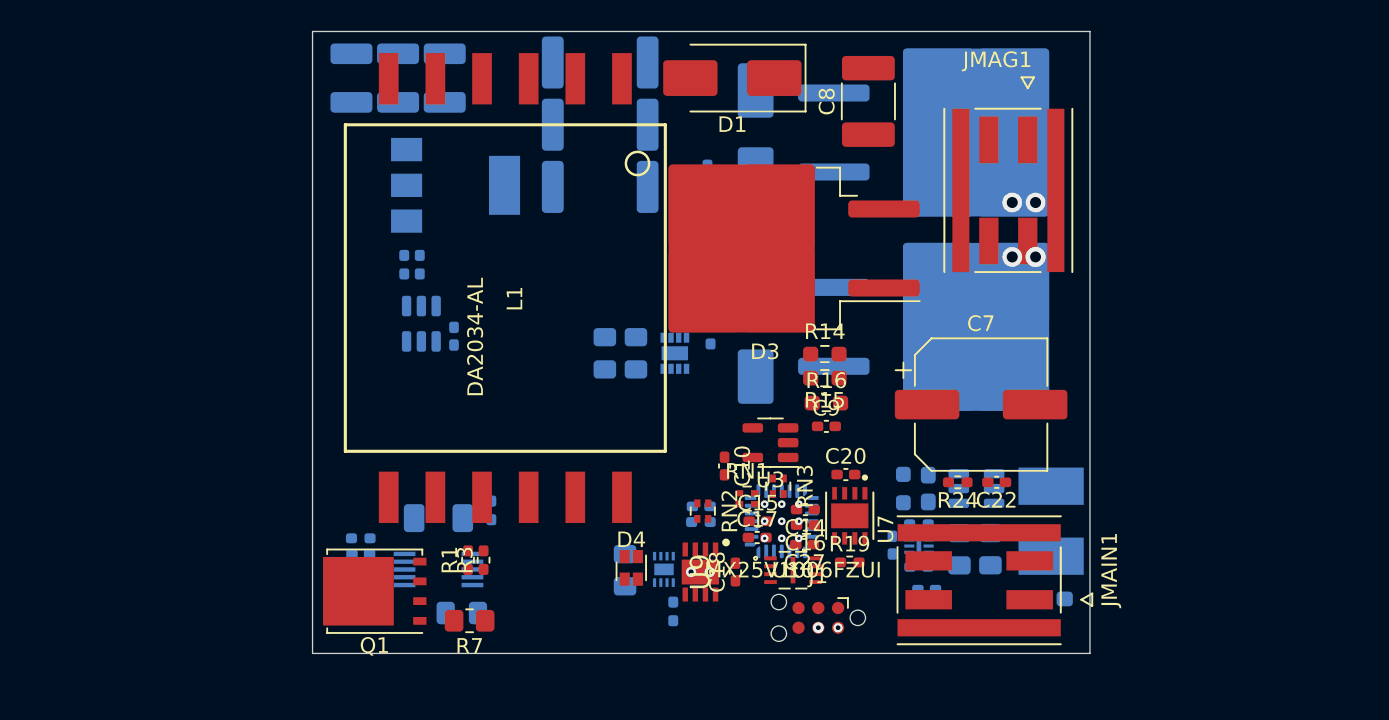
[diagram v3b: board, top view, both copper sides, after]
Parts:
- removed JCAP1: Molex 105429-1104, 1054291104:MOLEX_1054291104
- C10, C17, C27, C7, C9, R14, R15, R16, R19, U10, U3, U7: moved to F.Cu
- C12, C13, F1, U6: moved to B.Cu
- moved RN3 46.6 mm to (153.4, 114.2), turned to -90 degrees
- moved RN1 43.3 mm to (151.4, 115.0)
- moved RN2 42.2 mm to (148.6, 115.8), turned to -90 degrees
- moved C7 38.9 mm to (166.5, 109.0), turned to 0 degrees
- moved C29 29.8 mm to (160.8, 118.0), turned to 90 degrees
- moved FB2 28.4 mm to (161.5, 114.4), turned to 90 degrees
- moved C25 27.0 mm to (162.5, 119.4), turned to 180 degrees
- moved U11 26.5 mm to (162.5, 118.1), turned to 0 degrees
- moved R13 26.2 mm to (162.5, 116.7), turned to 0 degrees
- moved C24 25.3 mm to (163.1, 114.4), turned to -90 degrees
- moved D5 24.3 mm to (152.0, 91.5)
- moved D2 24.1 mm to (152.0, 104.5)
- moved R24 21.6 mm to (165.0, 114.0), turned to 180 degrees
- moved C26 21.4 mm to (165.1, 118.3), turned to -90 degrees
- moved U8 19.2 mm to (166.2, 114.4), turned to 0 degrees
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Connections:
- C8 pad 1: +3.3V -> VDC
- D1 pad 1: +3.3V -> VDC
- D3 pad 2: +3.3V -> VDC
- JMAG1 pad 1: /MAGNET_A_2 -> GND
- JMAG1 pad 2: /MAGNET_B_2 -> VDC
- JMAG1 pad 3: +3.3V -> /MAGNET_A_2
- JMAG1 pad 4: +3.3V -> /MAGNET_B_2
- JMAIN1 pad 1: /CAN_P -> Net-(F1-Pad1)
- JMAIN1 pad 2: /CAN_N -> GND
- JMAIN1 pad 3: Net-(F1-Pad1) -> /CAN_P
- JMAIN1 pad 4: GND -> /CAN_N
- R10 pad 1: +3.3V -> VDC
- R11 pad 1: +3.3V -> VDC
- R14 pad 1: +3.3V -> VDC
- R9 pad 1: +3.3V -> VDC
- RN1 pad 1: /Logic/CHARGE -> /Logic/DISCHARGE
- RN1 pad 2: /Logic/DISCHARGE -> /Logic/CHARGE
- RN2 pad 1: +3.3V -> /Logic/SCL
- RN2 pad 2: +3.3V -> /Logic/SDA
- RN2 pad 3: /Logic/SCL -> +3.3V
- RN2 pad 4: /Logic/SDA -> +3.3V
- RN3 pad 1: /Logic/KICK_B -> /Logic/KICK_A
- RN3 pad 2: /Logic/KICK_A -> /Logic/KICK_B
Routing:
- net (no net): track 224.5 -> 0.00 mm, vias 14 -> 0
- net GND: track 60.6 -> 0.00 mm, vias 21 -> 11
- net /Logic/DISCHARGE: track 22.2 -> 0.00 mm
- net /Logic/DONE: track 19.5 -> 0.00 mm
- net /Logic/CHARGE: track 19.5 -> 0.00 mm
- net /Logic/VOUT_ADC: track 17.6 -> 0.00 mm
- net Net-(D2-A1): track 15.6 -> 0.00 mm
- net +24V: track 15.1 -> 0.00 mm, vias 1 -> 0
- net Net-(Q2-D-Pad2): track 13.4 -> 0.00 mm
- net /Logic/KICK_B: track 11.2 -> 0.00 mm
- net /Logic/KICK_A: track 11.0 -> 0.00 mm
- net /Logic/SWDIO: track 10.8 -> 0.00 mm
- net Net-(D1-A): track 9.17 -> 0.00 mm
- net Net-(U4-NRST): track 8.39 -> 0.00 mm
- net /Logic/CAN_TX: track 7.17 -> 0.00 mm
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- added copper zone on In2.Cu, net +24V
- added copper zone on In2.Cu, net +3.3V
- added copper zone on In2.Cu, net +5V

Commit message: Finish the draft routing.
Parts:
- C19: moved to F.Cu
- moved C19 6.06 mm to (157.1, 119.5), turned to -90 degrees
- moved R12 4.27 mm to (127.1, 103.6), turned to -90 degrees
- moved C13 3.91 mm to (145.6, 103.6), turned to 180 degrees
- moved D4 3.10 mm to (144.8, 122.5)
- moved C1 3.10 mm to (136.1, 121.6), turned to -90 degrees
- moved R4 2.70 mm to (149.2, 107.2)
- moved U5 2.70 mm to (146.9, 108.4)
- moved FB2 2.70 mm to (161.5, 111.7), turned to -90 degrees
- moved R5 2.06 mm to (136.0, 117.6), turned to 180 degrees
- moved L2 1.70 mm to (171.0, 114.8)
- moved C11 1.48 mm to (147.0, 115.5)
- moved R22 1.48 mm to (147.0, 116.5)
- moved C10 1.36 mm to (151.2, 113.6), turned to 0 degrees
- moved R19 1.33 mm to (159.3, 119.6), turned to -90 degrees
- moved C21 1.30 mm to (145.6, 105.6), turned to 180 degrees
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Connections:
- JMAIN1 pad 3: /CAN_P -> /CAN_N
- JMAIN1 pad 4: /CAN_N -> /CAN_P
- RN2 pad 1: /Logic/SCL -> +3.3V
- RN2 pad 2: /Logic/SDA -> +3.3V
- RN2 pad 3: +3.3V -> /Logic/SDA
- RN2 pad 4: +3.3V -> /Logic/SCL
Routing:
- net GND: track 0.00 -> 72.9 mm, vias 11 -> 44
- net VDC: track 0.00 -> 56.5 mm, vias 0 -> 1
- net /Logic/DISCHARGE: track 0.00 -> 27.8 mm, vias 0 -> 1
- net /Power/RVOUT: track 0.00 -> 26.7 mm, vias 0 -> 1
- net +24V: track 0.00 -> 25.8 mm, vias 0 -> 8
- net /Logic/CHARGE: track 0.00 -> 21.8 mm, vias 0 -> 1
- net /Power/NMOS_DRAIN: track 0.00 -> 20.7 mm
- net /Logic/DONE: track 0.00 -> 20.2 mm
- net +3.3V: track 0.00 -> 19.0 mm, vias 0 -> 7
- net Net-(Q2-D-Pad2): track 0.00 -> 17.4 mm
- net Net-(U9-P0B): track 0.00 -> 16.9 mm
- net /Logic/SW_NRST: track 0.00 -> 16.2 mm, vias 0 -> 3
- net +5V: track 0.00 -> 15.7 mm, vias 0 -> 7
- net Net-(U5-OUT_B): track 0.00 -> 14.1 mm
- net /Logic/KICK_B: track 0.00 -> 11.3 mm, vias 0 -> 1
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- added copper zone on B.Cu, net GND
- added copper zone on F.Cu, net GND

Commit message: Move a lot of vias out of pads as this is an expensive option when manufacturing the PCB.
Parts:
- moved C22 3.41 mm to (170.9, 114.3)
- moved C18 2.66 mm to (149.2, 122.8), turned to 180 degrees
- moved D4 0.40 mm to (144.4, 122.5)
- moved C20 0.05 mm to (158.2, 113.5)
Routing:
- net GND: track 72.9 -> 98.1 mm, vias 44 -> 33
- net +24V: track 25.8 -> 31.9 mm
- net Net-(U8-BST): track 1.33 -> 4.76 mm
- net /Logic/SW_NRST: track 16.2 -> 19.2 mm
- net +3.3V: track 19.0 -> 22.0 mm
- net Net-(U8-IN): track 3.98 -> 6.51 mm
- net Net-(U8-EN): track 0.00 -> 2.49 mm
- net /Logic/SWCLK: track 6.40 -> 8.57 mm
- net /Logic/DISCHARGE: track 27.8 -> 29.7 mm
- net /Logic/SWDIO: track 6.45 -> 8.36 mm
- net Net-(D4-RK): track 1.94 -> 3.82 mm
- net Net-(U1-SOURCE): track 5.65 -> 7.49 mm
- net +5V: track 15.7 -> 17.3 mm
- net /Logic/CAN_RX: track 3.47 -> 5.05 mm
- net /Logic/SDA: track 7.58 -> 9.10 mm
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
